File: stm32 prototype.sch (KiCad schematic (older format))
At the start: 117 parts, among them J1 USB_B_Mini, J3 Conn_01x02, Q1 Q_NMOS_GSD, Q2 Q_NMOS_GSD, Q3 Q_NMOS_GSD, Q4 Q_NMOS_GSD, Q5 Q_NMOS_GSD, Q6 Q_NMOS_GSD, Q7 Q_NMOS_GSD, Q8 Q_NMOS_GSD, Q9 Q_NMOS_GSD, U1 FT232RL, U2 W25Q128JV-DTR, U3 STM32F407VGTx, U4 LD1117S33TR, U5 ESP32, U6 IS25LP016D-JNLE-TR, Y1 Crystal_GND24, Y2 Crystal_GND23, Y3 Crystal_GND23

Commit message: worked on some layout
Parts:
- added C16, C38: 2.2uF, Capacitors_SMD:C_0603, symbol Device:C
- added C39: .1uF, Capacitors_SMD:C_0603, symbol Device:C
- added C40: 1uF, Capacitors_SMD:C_0603, symbol Device:C
- added R46: DNP, Resistors_SMD:R_0603, symbol Device:R
- added R47: 10K, Resistors_SMD:R_0603, symbol Device:R
- C1, C10, C11, C12, C13, C14, C15, C17, C18, C19, C2, C20, C21, C22, C23, C24, C25, C26, C27, C28, C29, C3, C31, C36, C37, C4, C5, C6, C7, C8, C9: footprint Capacitors_SMD:C_0603_HandSoldering -> Capacitors_SMD:C_0603
- C41: renamed from C?; footprint Capacitors_SMD:C_0603_HandSoldering -> Capacitors_SMD:C_0603
- D10, D11, D2, D3, D4, D5, D6, D7, D8, D9: footprint LEDs:LED_1206_HandSoldering -> LEDs:LED_1206
- Q1, Q2, Q3, Q4, Q5, Q6, Q7, Q8: footprint TO_SOT_Packages_SMD:SOT-323_SC-70_Handsoldering -> TO_SOT_Packages_SMD:SOT-323_SC-70
- R1, R10, R11, R12, R13, R14, R15, R16, R17, R18, R19, R2, R20, R21, R22, R23, R24, R25, R3, R34, R35, R36, R4, R5, R6, R7, R8, R9: footprint Resistors_SMD:R_0603_HandSoldering -> Resistors_SMD:R_0603
- R40, R41, R42, R43, R44, R45, R48: renamed from R?; footprint Resistors_SMD:R_0603_HandSoldering -> Resistors_SMD:R_0603
- gave numbers to parts that had none: 1
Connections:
- net +3V3: now also U3.21 (VREF+), C39.2, C40.2, R46.1
- net GND: now also C16.1, C38.1, C39.1, C40.1, R47.1
- net at U3.49 (VCAP_1): now also C16.2
- net at U3.73 (VCAP_2): now also C38.2
- net at U3.94 (BOOT0): now also R46.2, R47.2

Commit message: laid out usb input section
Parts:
- added R49: 0R, Resistors_SMD:R_0603, symbol Device:R
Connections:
- net MEM_CHIP_SELECT: now also R49.1; no longer U2.1 (CE#)
- net at J1.3 (D+), U1.15 (USBD+): now also D1.2 (K); no longer D1.1 (K)
- net at J1.2 (D-), U1.16 (USBD-): now also D1.1 (K); no longer D1.2 (K)
- new net: R49.2, U2.1 (CE#)
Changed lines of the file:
@@
 	1    0    0    -1
 $EndComp
-Wire Wire Line
-	3550 9650 4050 9650
-Wire Wire Line
-	5200 9750 4250 9750
-Wire Wire Line
-	4050 10150 4050 9650
-Connection ~ 4050 9650
-Wire Wire Line
-	4050 9650 5200 9650
-Wire Wire Line
-	4250 10150 4250 9750
-Connection ~ 4250 9750
-Wire Wire Line
-	4250 9750 3550 9750
 $Comp
 L power:GND #PWR0109
@@
 	1    0    0    -1
 $EndComp
-Text GLabel 21000 5500 0    50   Input ~ 0
+Text GLabel 20550 5500 0    50   Input ~ 0
 MEM_CHIP_SELECT
 $Comp
@@
 Wire Wire Line
 	12300 6250 12050 6250
+$Comp
+L Device:R R49
+U 1 1 5C09E47A
+P 20700 5500
+F 0 "R49" V 20600 5500 50  0000 C CNN
+F 1 "0R" V 20700 5500 50  0000 C CNN
+F 2 "Resistors_SMD:R_0603" V 20630 5500 50  0001 C CNN
+F 3 "~" H 20700 5500 50  0001 C CNN
+	1    20700 5500
+	0    -1   1    0
+$EndComp
+Wire Wire Line
+	20850 5500 21000 5500
+Wire Wire Line
+	3550 9750 4050 9750
+Wire Wire Line
+	4250 10150 4250 9650
+Connection ~ 4250 9650
+Wire Wire Line
+	4250 9650 5200 9650
+Wire Wire Line
+	3550 9650 4250 9650
+Wire Wire Line
+	4050 10150 4050 9750
+Connection ~ 4050 9750
+Wire Wire Line
+	4050 9750 5200 9750
 $EndSCHEMATC

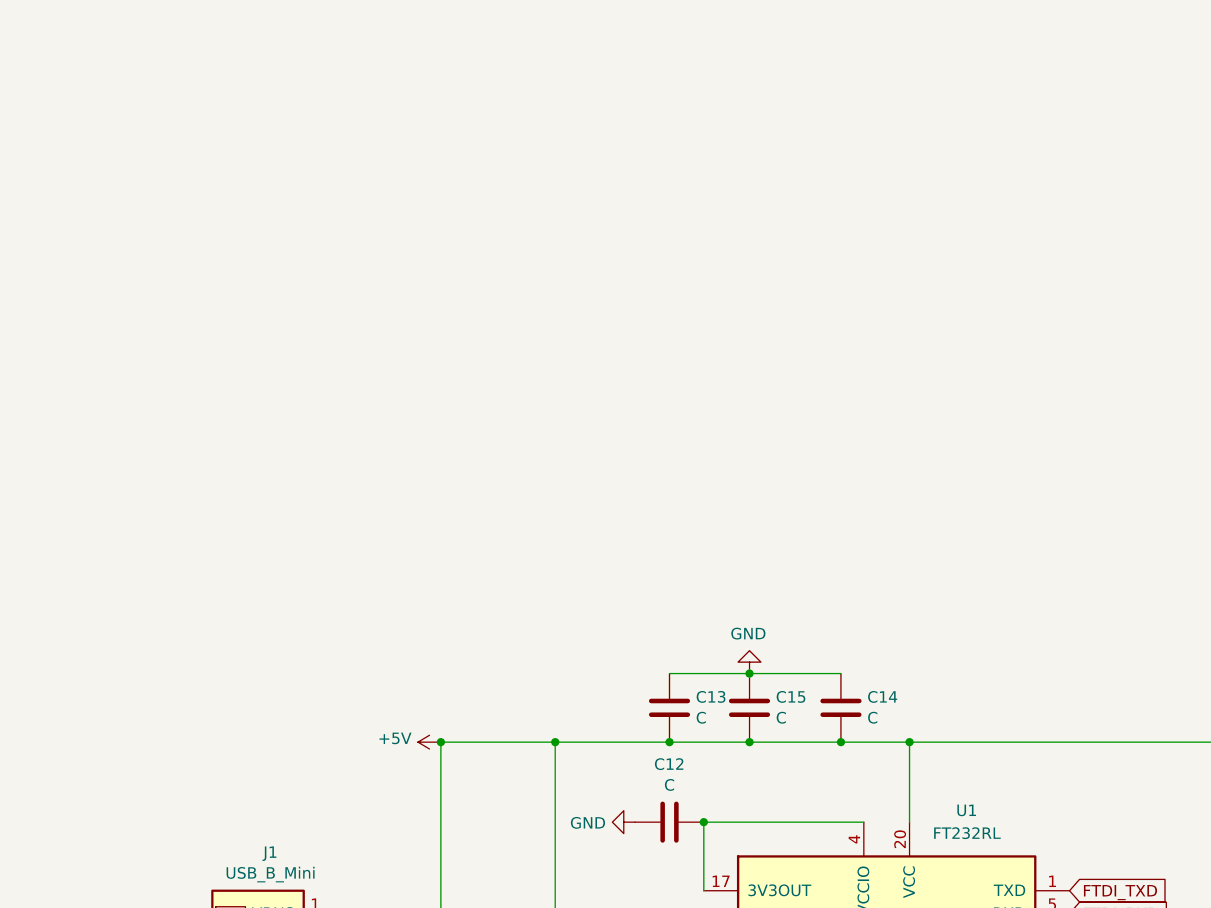
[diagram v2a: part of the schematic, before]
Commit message: added switcher to 3.3v rail, began layout of 3.3v regulator
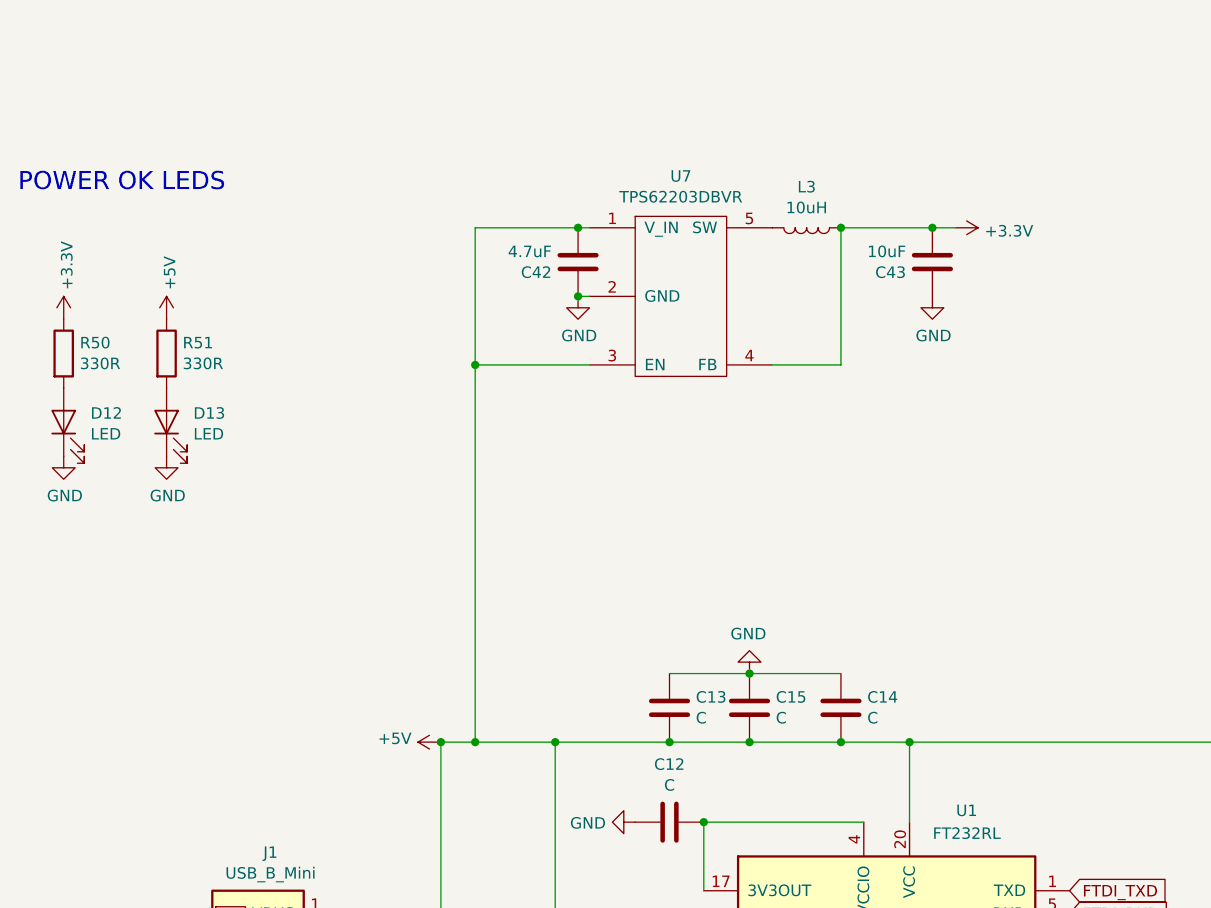
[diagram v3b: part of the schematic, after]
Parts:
- added C42: 4.7uF, Capacitors_SMD:C_0603, symbol Device:C
- added C43: 10uF, Capacitors_SMD:C_0603, symbol Device:C
- added D12, D13: LED, LEDs:LED_1206, symbol Device:LED
- added L3: 10uH, Inductors_SMD:L_1210, symbol Device:L
- added R50, R51: 330R, Resistors_SMD:R_0603, symbol Device:R
- added U7: TPS62203DBVR, digikey-footprints:SOT-753, symbol voltage_regulators_mdg:TPS62203DBVR
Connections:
- net +3V3: now also C43.1, L3.1, R50.1, U7.4 (FB)
- net +5V: now also C42.1, R51.1, U7.1 (V_IN), U7.3 (EN)
- net GND: now also C42.2, C43.2, D12.1 (K), D13.1 (K), U7.2 (GND)
- new net: L3.2, U7.5 (SW)
- new net: D12.2 (A), R50.2
- new net: D13.2 (A), R51.2
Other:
- note added: "POWER OK LEDS"
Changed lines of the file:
@@
 	4050 9450 4050 8700
 Wire Wire Line
-	4050 8700 4550 8700
+	4050 8700 4200 8700
 Connection ~ 5400 8700
 Wire Wire Line
@@
 Wire Wire Line
 	4050 9750 5200 9750
+$Comp
+L voltage_regulators_mdg:TPS62203DBVR U7
+U 1 1 5C0E9CAA
+P 5100 6750
+F 0 "U7" H 5100 7275 50  0000 C CNN
+F 1 "TPS62203DBVR" H 5100 7184 50  0000 C CNN
+F 2 "digikey-footprints:SOT-753" H 5100 6750 50  0001 C CNN
+F 3 "" H 5100 6750 50  0001 C CNN
+	1    5100 6750
+	1    0    0    -1
+$EndComp
+Wire Wire Line
+	4700 6450 4650 6450
+Connection ~ 4200 8700
+Wire Wire Line
+	4200 8700 4550 8700
+Wire Wire Line
+	4700 7050 4200 7050
+$Comp
+L power:GND #PWR0148
+U 1 1 5C11C8B8
+P 4650 6750
+F 0 "#PWR0148" H 4650 6500 50  0001 C CNN
+F 1 "GND" H 4655 6577 50  0000 C CNN
+F 2 "" H 4650 6750 50  0001 C CNN
+F 3 "" H 4650 6750 50  0001 C CNN
+	1    4650 6750
+	1    0    0    -1
+$EndComp
+$Comp
+L Device:C C42
+U 1 1 5C11E324
+P 4650 6600
+F 0 "C42" H 4535 6554 50  0000 R CNN
+F 1 "4.7uF" H 4535 6645 50  0000 R CNN
+F 2 "Capacitors_SMD:C_0603" H 4688 6450 50  0001 C CNN
+F 3 "~" H 4650 6600 50  0001 C CNN
+	1    4650 6600
+	1    0    0    -1
+$EndComp
+Connection ~ 4650 6450
+Wire Wire Line
+	4650 6450 4200 6450
+Wire Wire Line
+	4700 6750 4650 6750
+Connection ~ 4650 6750
+$Comp
+L Device:L L3
+U 1 1 5C143E12
+P 5650 6450
+F 0 "L3" V 5472 6450 50  0000 C CNN
+F 1 "10uH" V 5563 6450 50  0000 C CNN
+F 2 "Inductors_SMD:L_1210" H 5650 6450 50  0001 C CNN
+F 3 "~" H 5650 6450 50  0001 C CNN
+F 4 " LBC3225T100KR " V 5650 6450 50  0001 C CNN "Part Number"
+	1    5650 6450
+	0    1    1    0
+$EndComp
+Wire Wire Line
+	5500 7050 5800 7050
+Wire Wire Line
+	5800 7050 5800 6450
+$Comp
+L Device:C C43
+U 1 1 5C156EBA
+P 6200 6600
+F 0 "C43" H 6085 6554 50  0000 R CNN
+F 1 "10uF" H 6085 6645 50  0000 R CNN
+F 2 "Capacitors_SMD:C_0603" H 6238 6450 50  0001 C CNN
+F 3 "~" H 6200 6600 50  0001 C CNN
+	1    6200 6600
+	1    0    0    -1
+$EndComp
+Connection ~ 5800 6450
+$Comp
+L power:GND #PWR0149
+U 1 1 5C168BBB
+P 6200 6750
+F 0 "#PWR0149" H 6200 6500 50  0001 C CNN
+F 1 "GND" H 6205 6577 50  0000 C CNN
+F 2 "" H 6200 6750 50  0001 C CNN
+F 3 "" H 6200 6750 50  0001 C CNN
+	1    6200 6750
+	1    0    0    -1
+$EndComp
+$Comp
+L power:+3.3V #PWR0150
+U 1 1 5C18E015
+P 6300 6450
+F 0 "#PWR0150" H 6300 6300 50  0001 C CNN
+F 1 "+3.3V" V 6315 6578 50  0000 L CNN
+F 2 "" H 6300 6450 50  0001 C CNN
+F 3 "" H 6300 6450 50  0001 C CNN
+	1    6300 6450
+	0    1    1    0
+$EndComp
+Connection ~ 6200 6450
+Wire Wire Line
+	6200 6450 6300 6450
+Wire Wire Line
+	5800 6450 6200 6450
+Wire Wire Line
+	4200 6450 4200 7050
+Connection ~ 4200 7050
+Wire Wire Line
+	4200 7050 4200 8700
+$Comp
+L power:+3.3V #PWR0151
+U 1 1 5C1C9A2E
+P 2400 6850
+F 0 "#PWR0151" H 2400 6700 50  0001 C CNN
+F 1 "+3.3V" V 2415 6978 50  0000 L CNN
+F 2 "" H 2400 6850 50  0001 C CNN
+F 3 "" H 2400 6850 50  0001 C CNN
+	1    2400 6850
+	1    0    0    -1
+$EndComp
+$Comp
+L Device:R R50
+U 1 1 5C1CB9B9
+P 2400 7000
+F 0 "R50" H 2470 7046 50  0000 L CNN
+F 1 "330R" H 2470 6955 50  0000 L CNN
+F 2 "Resistors_SMD:R_0603" V 2330 7000 50  0001 C CNN
+F 3 "~" H 2400 7000 50  0001 C CNN
+	1    2400 7000
+	1    0    0    -1
+$EndComp
+$Comp
+L Device:LED D12
+U 1 1 5C1CD911
+P 2400 7300
+F 0 "D12" V 2438 7183 50  0000 R CNN
+F 1 "LED" V 2347 7183 50  0000 R CNN
+F 2 "LEDs:LED_1206" H 2400 7300 50  0001 C CNN
+F 3 "~" H 2400 7300 50  0001 C CNN
+	1    2400 7300
+	0    -1   -1   0
+$EndComp
+$Comp
+L power:GND #PWR0152
+U 1 1 5C1CEBAF
+P 2400 7450
+F 0 "#PWR0152" H 2400 7200 50  0001 C CNN
+F 1 "GND" H 2405 7277 50  0000 C CNN
+F 2 "" H 2400 7450 50  0001 C CNN
+F 3 "" H 2400 7450 50  0001 C CNN
+	1    2400 7450
+	1    0    0    -1
+$EndComp
+$Comp
+L Device:R R51
+U 1 1 5C1CF4E3
+P 2850 7000
+F 0 "R51" H 2920 7046 50  0000 L CNN
+F 1 "330R" H 2920 6955 50  0000 L CNN
+F 2 "Resistors_SMD:R_0603" V 2780 7000 50  0001 C CNN
+F 3 "~" H 2850 7000 50  0001 C CNN
+	1    2850 7000
+	1    0    0    -1
+$EndComp
+$Comp
+L Device:LED D13
+U 1 1 5C1CF4EA
+P 2850 7300
+F 0 "D13" V 2888 7183 50  0000 R CNN
+F 1 "LED" V 2797 7183 50  0000 R CNN
+F 2 "LEDs:LED_1206" H 2850 7300 50  0001 C CNN
+F 3 "~" H 2850 7300 50  0001 C CNN
+	1    2850 7300
+	0    -1   -1   0
+$EndComp
+$Comp
+L power:GND #PWR0153
+U 1 1 5C1CF4F1
+P 2850 7450
+F 0 "#PWR0153" H 2850 7200 50  0001 C CNN
+F 1 "GND" H 2855 7277 50  0000 C CNN
+F 2 "" H 2850 7450 50  0001 C CNN
+F 3 "" H 2850 7450 50  0001 C CNN
+	1    2850 7450
+	1    0    0    -1
+$EndComp
+$Comp
+L power:+5V #PWR0154
+U 1 1 5C1E6B08
+P 2850 6850
+F 0 "#PWR0154" H 2850 6700 50  0001 C CNN
+F 1 "+5V" V 2865 6978 50  0000 L CNN
+F 2 "" H 2850 6850 50  0001 C CNN
+F 3 "" H 2850 6850 50  0001 C CNN
+	1    2850 6850
+	1    0    0    -1
+$EndComp
+Text Notes 2200 6300 0    79   ~ 0
+POWER OK LEDS
 $EndSCHEMATC

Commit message: worked on some layout around the stm32f
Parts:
- added J4: Conn_01x10, Pin_Headers:Pin_Header_Straight_1x10_Pitch2.54mm, symbol Connector_Generic:Conn_01x10
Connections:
- net +3V3: now also J4.9 (Pin_9)
- net +5V: now also J4.8 (Pin_8)
- net GND: now also J4.10 (Pin_10)
- net STATUS_BIT0: now also U3.46 (PE15)
- net STATUS_BIT1: now also U3.45 (PE14)
- net STATUS_BIT2: now also U3.44 (PE13)
- net STATUS_BIT3: now also U3.43 (PE12)
- net STATUS_BIT4: now also U3.42 (PE11)
- net STATUS_BIT5: now also U3.41 (PE10)
- net STATUS_BIT6: now also U3.40 (PE9)
- net STATUS_BIT7: now also U3.39 (PE8)
- net FTDI_DCD: now reaches U1.10 (DCD)
- net FTDI_DCD: now also J4.4 (Pin_4)
- net FTDI_CBUS4: now reaches U1.12 (CBUS4)
- net FTDI_CBUS4: now also J4.5 (Pin_5)
- net FTDI_CBUS2: now reaches U1.13 (CBUS2)
- net FTDI_CBUS2: now also J4.6 (Pin_6)
- net FTDI_CBUS3: now reaches U1.14 (CBUS3)
- net FTDI_CBUS3: now also J4.7 (Pin_7)
- net FTDI_DTR: now reaches U1.2 (DTR)
- net FTDI_DTR: now also J4.1 (Pin_1)
- net FTDI_RI: now reaches U1.6 (RI)
- net FTDI_RI: now also J4.2 (Pin_2)
- net FTDI_DCR: now reaches U1.9 (DCR)
- net FTDI_DCR: now also J4.3 (Pin_3)
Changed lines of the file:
@@
 Text Notes 2200 6300 0    79   ~ 0
 POWER OK LEDS
+Text GLabel 14450 8650 0    50   Input ~ 0
+STATUS_BIT0
+Text GLabel 14450 8550 0    50   Input ~ 0
+STATUS_BIT1
+Text GLabel 14450 8450 0    50   Input ~ 0
+STATUS_BIT2
+Text GLabel 14450 8350 0    50   Input ~ 0
+STATUS_BIT3
+Text GLabel 14450 8250 0    50   Input ~ 0
+STATUS_BIT4
+Text GLabel 14450 8150 0    50   Input ~ 0
+STATUS_BIT5
+Text GLabel 14450 8050 0    50   Input ~ 0
+STATUS_BIT6
+Text GLabel 14450 7950 0    50   Input ~ 0
+STATUS_BIT7
+$Comp
+L Connector_Generic:Conn_01x10 J4
+U 1 1 5C3119D0
+P 9500 10150
+F 0 "J4" H 9580 10142 50  0000 L CNN
+F 1 "Conn_01x10" H 9580 10051 50  0000 L CNN
+F 2 "Pin_Headers:Pin_Header_Straight_1x10_Pitch2.54mm" H 9500 10150 50  0001 C CNN
+F 3 "~" H 9500 10150 50  0001 C CNN
+	1    9500 10150
+	1    0    0    -1
+$EndComp
+Text GLabel 6800 9750 2    50   Input ~ 0
+FTDI_DTR
+Text GLabel 6800 9850 2    50   Input ~ 0
+FTDI_DCR
+Text GLabel 6800 9950 2    50   Input ~ 0
+FTDI_DCD
+Text GLabel 6800 10050 2    50   Input ~ 0
+FTDI_RI
+Text GLabel 6800 10550 2    50   Input ~ 0
+FTDI_CBUS2
+Text GLabel 6800 10650 2    50   Input ~ 0
+FTDI_CBUS3
+Text GLabel 6800 10750 2    50   Input ~ 0
+FTDI_CBUS4
+Text GLabel 9300 9750 0    50   Input ~ 0
+FTDI_DTR
+Text GLabel 9300 9850 0    50   Input ~ 0
+FTDI_RI
+Text GLabel 9300 9950 0    50   Input ~ 0
+FTDI_DCR
+Text GLabel 9300 10050 0    50   Input ~ 0
+FTDI_DCD
+Text GLabel 9300 10150 0    50   Input ~ 0
+FTDI_CBUS4
+Text GLabel 9300 10250 0    50   Input ~ 0
+FTDI_CBUS2
+Text GLabel 9300 10350 0    50   Input ~ 0
+FTDI_CBUS3
+$Comp
+L power:+5V #PWR0155
+U 1 1 5C3158AD
+P 9300 10450
+F 0 "#PWR0155" H 9300 10300 50  0001 C CNN
+F 1 "+5V" V 9315 10578 50  0000 L CNN
+F 2 "" H 9300 10450 50  0001 C CNN
+F 3 "" H 9300 10450 50  0001 C CNN
+	1    9300 10450
+	0    -1   -1   0
+$EndComp
+$Comp
+L power:+3.3V #PWR0156
+U 1 1 5C315DEA
+P 9300 10550
+F 0 "#PWR0156" H 9300 10400 50  0001 C CNN
+F 1 "+3.3V" V 9315 10678 50  0000 L CNN
+F 2 "" H 9300 10550 50  0001 C CNN
+F 3 "" H 9300 10550 50  0001 C CNN
+	1    9300 10550
+	0    -1   -1   0
+$EndComp
+$Comp
+L power:GND #PWR0157
+U 1 1 5C316BFC
+P 9300 10650
+F 0 "#PWR0157" H 9300 10400 50  0001 C CNN
+F 1 "GND" H 9305 10477 50  0000 C CNN
+F 2 "" H 9300 10650 50  0001 C CNN
+F 3 "" H 9300 10650 50  0001 C CNN
+	1    9300 10650
+	1    0    0    -1
+$EndComp
 $EndSCHEMATC

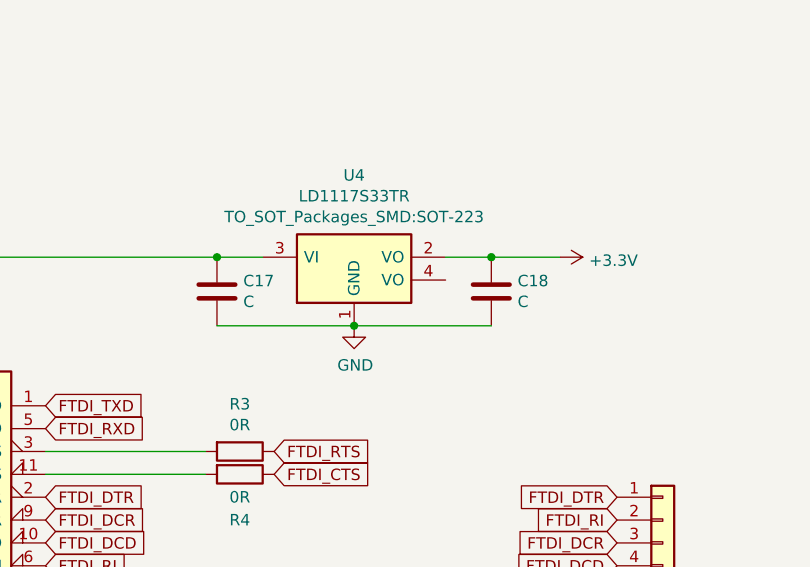
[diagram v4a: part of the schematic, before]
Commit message: laid out reserve linear 3.3V regulator, wired up FTDI header
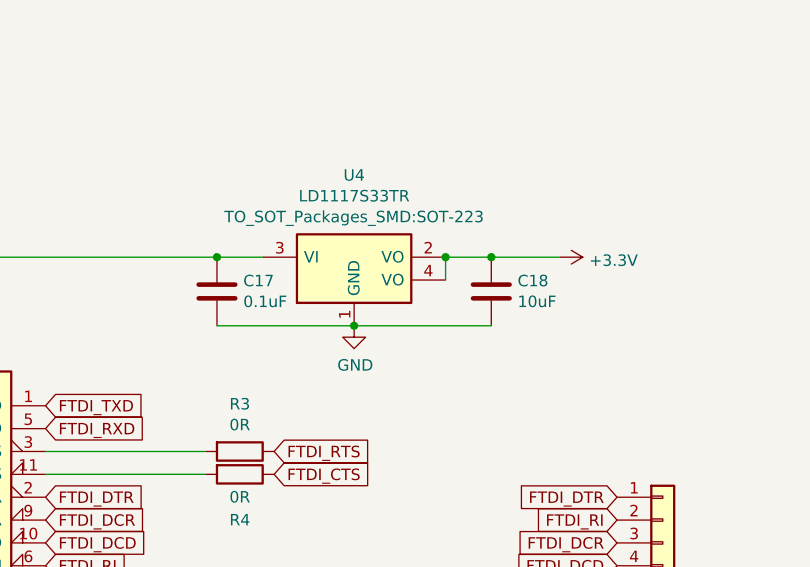
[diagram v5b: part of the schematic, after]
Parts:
- C17: value C -> 0.1uF
- C18: value C -> 10uF
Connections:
- net +3V3: now also U4.4 (VO)
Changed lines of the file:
@@
 P 7550 8850
 F 0 "C17" H 7435 8804 50  0000 R CNN
-F 1 "C" H 7435 8895 50  0000 R CNN
+F 1 "0.1uF" H 7435 8895 50  0000 R CNN
 F 2 "Capacitors_SMD:C_0603" H 7588 8700 50  0001 C CNN
 F 3 "~" H 7550 8850 50  0001 C CNN
@@
 P 8750 8850
 F 0 "C18" H 8635 8804 50  0000 R CNN
-F 1 "C" H 8635 8895 50  0000 R CNN
+F 1 "10uF" H 8635 8895 50  0000 R CNN
 F 2 "Capacitors_SMD:C_0603" H 8788 8700 50  0001 C CNN
 F 3 "~" H 8750 8850 50  0001 C CNN
@@
 	1    0    0    -1
 $EndComp
+Wire Wire Line
+	8550 8800 8550 8700
+Connection ~ 8550 8700
 $EndSCHEMATC
